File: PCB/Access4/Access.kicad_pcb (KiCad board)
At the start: 2 copper layers, 57.8 x 27 mm, 76 parts, among them J1 USB-C, J2 RFID, J3 INPUTS, J4 Shelly, J5 POWER, J6 DOOR2, J7 DOOR1, Q1 NX7002AK, Q2 PMF250XNEX, SW1 ESE13V01D, U1 ESP32-PICO-MINI-02, U2 FT231XQ, U3 G3VM-41GR8, U4 LMR16006XDDCR, U5 LMR16006XDDCR, U6 AA, U7 QR, U8 G3VM-41GR8, U9 AA

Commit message: Started on Access4
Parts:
- removed C10, C13: 2.2uF, RevK:C_0805_
- removed C11, C14: 10uF, RevK:C_0805_
- removed C12, C9: 100nF, RevK:C_0603_
- removed D6, D7: Schottky, RevK:D_1206_
- removed J4: Shelly, RevK:Shelly
- removed L1, L2: 6.8uH, RevK:L_4x4_
- removed Q1: NX7002AK, Package_TO_SOT_SMD:SOT-23
- removed R20: 100K, RevK:R_0603
- removed R21, R22: 100k 1%, RevK:R_0603
- removed R23: 18k 1%, RevK:R_0603
- removed R24: 30k 1%, RevK:R_0603
- removed R3: 10k, RevK:R_0603
- removed U4, U5: LMR16006XDDCR, RevK:SOT-23-Thin-6-Reg
- added C18: 100nF, RevK:C_0402, F.Cu at (58.9, 101.5)
- added C19: 22uF, RevK:C_0402, F.Cu at (58.9, 103.3)
- added C20: 1uF, RevK:C_0402, F.Cu at (58.9, 105.1)
- added C21: 10uF 50V, RevK:C_0603_, F.Cu at (59.0, 95.8)
- added C22: 10uF 6.3V, RevK:C_0603_, F.Cu at (59.0, 97.7)
- added C23: 100nF, RevK:C_0603_, F.Cu at (59.0, 99.6)
- added J8: Shelly, RevK:Shelly, F.Cu at (47.2, 107.9)
- added L3: 10uH, RevK:L_4x4_, F.Cu at (60.2, 87.1)
- added L4: 10uH, RevK:L_4x4_, F.Cu at (60.2, 92.2)
- added PCB1: 70x70, RevK:PCB7070, F.Cu at (98.0, 102.0)
- added R26: 10K, RevK:R_0402, F.Cu at (61.5, 101.5)
- added R27: 1M, RevK:R_0402_, F.Cu at (61.5, 103.3)
- added U10: ESP32-S3-MINI-1, RevK:ESP32-S3-MINI-1, F.Cu at (91.9, 125.3)
- added V1: ~, RevK:VCUT70, F.Cu at (103.0, 62.4)
- added V2: ~, RevK:VCUT70, F.Cu at (103.0, 64.7)
- C1: value 0.1uF -> 10uF 50V; footprint RevK:C_0603 -> RevK:C_0603_
- C15: value 1uF -> 10uF 6.3V; footprint RevK:C_0603 -> RevK:C_0603_
- C16: value 10nF -> 100nF; footprint RevK:C_0603 -> RevK:C_0603_
- C2, C3, C4, C5, C6, C7, C8, D1, D2, D3, D4: moved to F.Cu
- R1: value 10k -> 124k; footprint RevK:R_0603 -> RevK:R_0402_
- R14: value 27R -> 124k; footprint RevK:R_0603 -> RevK:R_0402_
- R15: value 27R -> 39k2; footprint RevK:R_0603 -> RevK:R_0402_
- R2: value 4k7 -> 23k2; footprint RevK:R_0603 -> RevK:R_0402_
- U1: value ESP32-PICO-MINI-02 -> MD8942; footprint RevK:ESP32-PICO-MINI-02 -> RevK:SOT-23-6-MD8942
- U2: value FT231XQ -> MD8942; footprint RevK:QFN-20-1EP_4x4mm_P0.5mm_EP2.5x2.5mm -> RevK:SOT-23-6-MD8942
- moved D1 69.4 mm to (49.5, 81.2), turned to 180 degrees
- moved C2 67.4 mm to (50.5, 78.7)
- moved C3 63.5 mm to (52.5, 78.7)
- moved D2 61.5 mm to (53.5, 81.2), turned to 180 degrees
- moved C4 59.6 mm to (54.5, 78.7)
- moved C5 55.6 mm to (56.5, 78.7)
- moved D3 53.7 mm to (57.5, 81.2), turned to 180 degrees
- moved C6 51.7 mm to (58.5, 78.7)
- moved C7 47.8 mm to (60.5, 78.7)
- moved D4 45.9 mm to (61.5, 81.2), turned to 180 degrees
- moved U2 45.3 mm to (125.3, 125.5)
- moved C8 43.9 mm to (62.5, 78.7)
- moved U1 40.0 mm to (112.0, 125.7)
- moved C17 38.5 mm to (118.1, 98.4)
- moved AJK1 38.5 mm to (77.6, 106.8)
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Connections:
- J1 pad A6: Net-(J1-D+-PadA6) -> D+
- J1 pad A7: Net-(J1-D--PadA7) -> D-
- J1 pad B6: Net-(J1-D+-PadA6) -> D+
- J1 pad B7: Net-(J1-D--PadA7) -> D-
- U1 pad 1: GND -> unconnected-(U1-Pad1)
- U1 pad 3: +3.3V -> unconnected-(U1-Pad3)
- U1 pad 4: unconnected-(U1-I36-Pad4) -> SHDN
- U1 pad 5: unconnected-(U1-I37-Pad5) -> +12V
- U1 pad 7: unconnected-(U1-I39-Pad7) -> GND
- U1 pad 8: EN -> +5V
- U2 pad 1: O -> unconnected-(U2-Pad1)
- U2 pad 3: GND -> unconnected-(U2-Pad3)
- U2 pad 4: GND -> unconnected-(U2-EN-Pad4)
- U2 pad 5: GND -> +12V
- U2 pad 6: GND -> unconnected-(U2-Pad6)
- U2 pad 7: Net-(U2-CBUS2) -> GND
- U2 pad 8: D+ -> +3.3V
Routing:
- net +3.3V: track 156.1 -> 0.00 mm, vias 10 -> 0
- net +12V: track 69.4 -> 0.00 mm, vias 2 -> 0
- net I: track 58.5 -> 0.00 mm, vias 2 -> 0
- net O: track 57.1 -> 0.00 mm, vias 2 -> 0
- net BOOT: track 54.3 -> 0.00 mm, vias 2 -> 0
- net R: track 43.2 -> 0.00 mm, vias 2 -> 0
- net B: track 42.0 -> 0.00 mm, vias 2 -> 0
- net G: track 40.3 -> 0.00 mm, vias 2 -> 0
- net GND: track 36.2 -> 0.00 mm, vias 13 -> 0
- net EN: track 35.8 -> 0.00 mm, vias 2 -> 0
- net RELAY1: track 34.5 -> 0.00 mm, vias 2 -> 0
- net RELAY2: track 32.1 -> 0.00 mm, vias 2 -> 0
- net TAMPER: track 29.5 -> 0.00 mm, vias 2 -> 0
- net Net-(Q1-D): track 27.5 -> 0.00 mm, vias 2 -> 0
- net +5V: track 25.3 -> 0.00 mm, vias 2 -> 0
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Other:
- board size 57.8 x 27 mm -> 70 x 70 mm

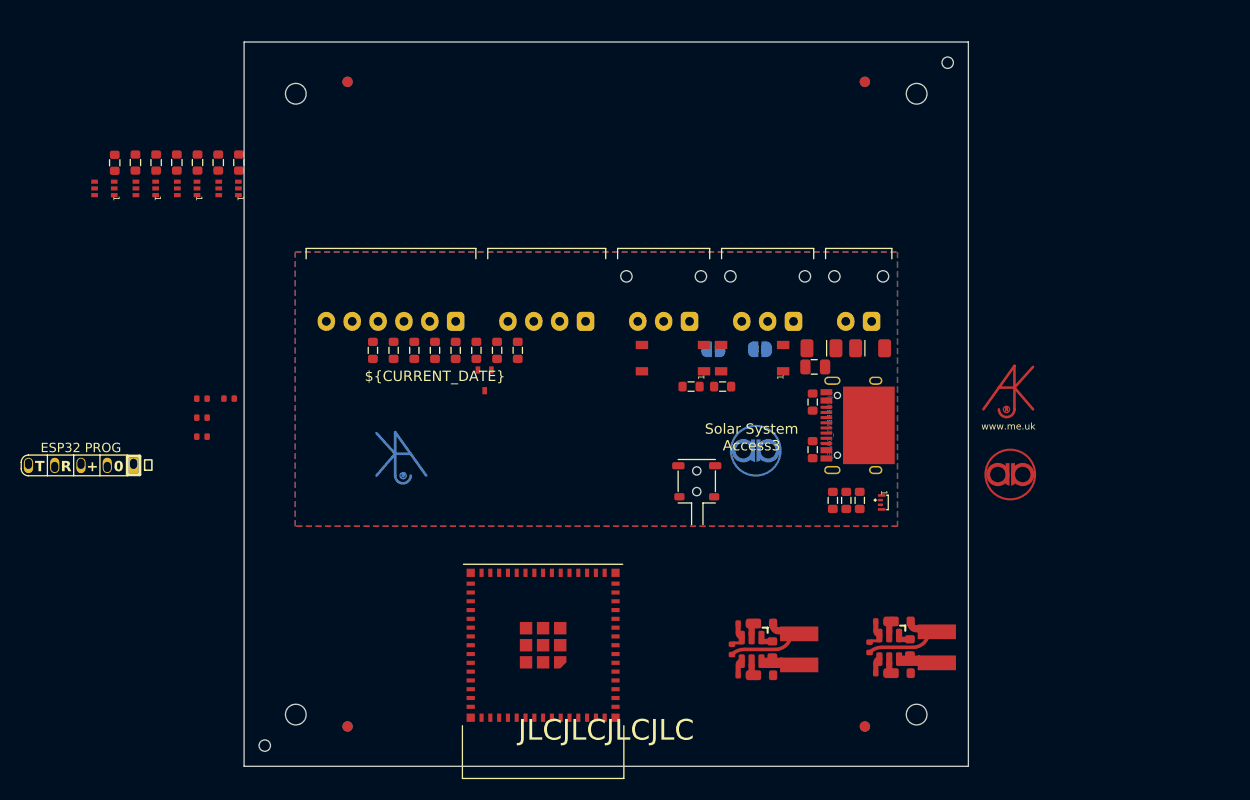
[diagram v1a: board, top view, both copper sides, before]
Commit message: Basic size and placement
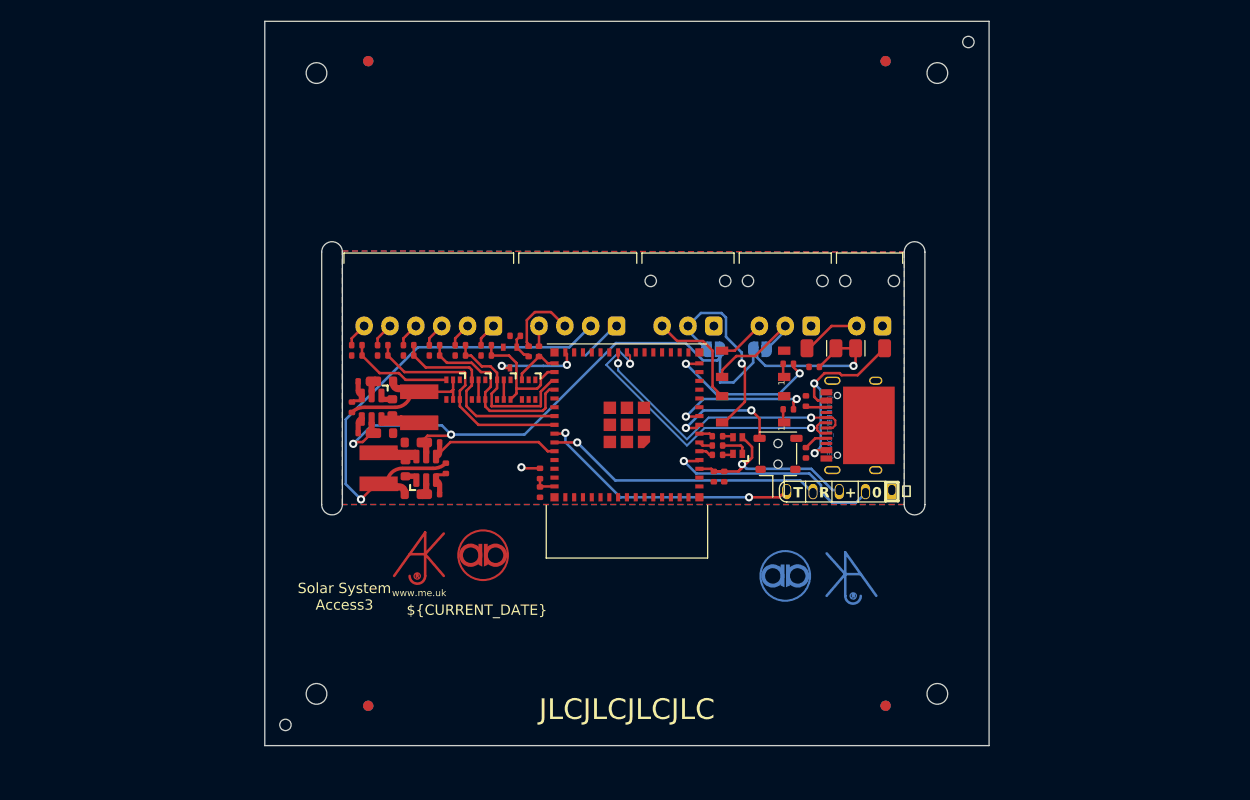
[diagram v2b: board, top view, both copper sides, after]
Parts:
- removed D5: LED_BARG, RevK:MHS190RGBCT
- removed R17: 300R, RevK:R_0603
- removed R18: 1K, RevK:R_0603
- removed R19: 100R, RevK:R_0603
- added D6: RGB, RevK:LED-RGB-1.6x1.6, F.Cu at (110.7, 106.0)
- added R20: 2K, RevK:R_0402, F.Cu at (108.8, 106.9)
- added R21: 220R, RevK:R_0402, F.Cu at (108.8, 105.1)
- added R3: 680R, RevK:R_0402, F.Cu at (108.8, 106.0)
- C17: footprint RevK:C_0805 -> RevK:C_0402
- C2, C3, C4, C5, C6, C7, C8: footprint RevK:C_0603 -> RevK:C_0402
- D1, D2, D3, D4: footprint Package_TO_SOT_SMD:SOT-363_SC-70-6 -> RevK:SOT-363_SC-70-6
- R10, R11, R12, R13, R16, R25, R4, R5, R6, R7, R8, R9: footprint RevK:R_0603 -> RevK:R_0402
- moved J8 73.3 mm to (120.5, 110.5)
- moved Logo1 59.2 mm to (80.5, 116.5)
- moved U2 55.1 mm to (75.3, 102.3)
- moved U9 51.5 mm to (86.1, 116.6)
- moved C19 50.8 mm to (109.4, 109.0), turned to -90 degrees
- moved C18 50.0 mm to (108.4, 109.0), turned to -90 degrees
- moved V2 47.1 mm to (100.0, 111.7), turned to 180 degrees
- moved D1 45.4 mm to (90.5, 100.6), turned to -90 degrees
- moved AJK1 45.0 mm to (121.1, 118.4)
- moved C2 42.2 mm to (89.2, 95.4), turned to 0 degrees
- moved D2 39.7 mm to (88.1, 100.6), turned to -90 degrees
- moved C16 39.6 mm to (52.0, 100.0)
- moved C3 38.7 mm to (86.4, 97.3), turned to 180 degrees
- moved U1 36.0 mm to (80.6, 108.2), turned to -90 degrees
- moved C4 34.8 mm to (83.9, 97.3), turned to 180 degrees
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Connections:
- U10 pad 15: unconnected-(U10-GPIO11-Pad15) -> RELAY1
- U10 pad 30: unconnected-(U10-GPIO48-Pad30) -> RFRX
- U10 pad 31: unconnected-(U10-GPIO35-Pad31) -> RFTX
- U10 pad 32: unconnected-(U10-GPIO36-Pad32) -> IO1
- U10 pad 33: unconnected-(U10-GPIO37-Pad33) -> IO2
- U10 pad 34: unconnected-(U10-GPIO38-Pad34) -> IO3
- U10 pad 35: unconnected-(U10-GPIO39-Pad35) -> IO4
- U10 pad 36: unconnected-(U10-GPIO40-Pad36) -> IO5
- U10 pad 37: unconnected-(U10-GPIO41-Pad37) -> IO6
- U10 pad 41: unconnected-(U10-GPIO45-Pad41) -> SHDN
- U10 pad 5: unconnected-(U10-GPIO1-Pad5) -> G
- U10 pad 6: unconnected-(U10-GPIO2-Pad6) -> R
- U10 pad 7: unconnected-(U10-GPIO3-Pad7) -> B
- U10 pad 8: unconnected-(U10-GPIO4-Pad8) -> TAMPER
- U10 pad 9: unconnected-(U10-GPIO5-Pad9) -> RELAY2
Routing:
- net +12V: track 0.00 -> 72.5 mm, vias 0 -> 3
- net +5V: track 0.00 -> 38.1 mm, vias 0 -> 1
- net D-: track 0.00 -> 31.4 mm, vias 0 -> 2
- net +3.3V: track 0.00 -> 31.3 mm, vias 0 -> 2
- net D+: track 0.00 -> 27.9 mm, vias 0 -> 2
- net Net-(J8-Rx): track 0.00 -> 27.0 mm, vias 0 -> 1
- net Net-(J8-Tx): track 0.00 -> 25.9 mm, vias 0 -> 2
- net IO5: track 0.00 -> 22.5 mm
- net Net-(J8-0): track 0.00 -> 21.5 mm, vias 0 -> 1
- net IO4: track 0.00 -> 19.8 mm
- net VBUS: track 0.00 -> 19.5 mm, vias 0 -> 2
- net Net-(J6-Pin_2): track 0.00 -> 19.3 mm, vias 0 -> 1
- net IO3: track 0.00 -> 18.6 mm
- net IO2: track 0.00 -> 16.1 mm
- net RELAY1: track 0.00 -> 15.6 mm, vias 0 -> 2
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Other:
- board text removed: "-"
- board text removed: "Door Closed"
- board text removed: "Exit Button"
- board text removed: "Lock Engaged"
- board text removed: "Power"

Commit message: Basic layout better
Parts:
- moved D4 8.03 mm to (87.3, 107.5), turned to 0 degrees
- moved D3 4.79 mm to (87.3, 105.1), turned to 0 degrees
- moved D1 3.21 mm to (87.3, 100.3), turned to 0 degrees
- moved D2 2.25 mm to (87.3, 102.7), turned to 0 degrees
- moved U9 1.61 mm to (87.5, 117.4)
- moved C8 0.30 mm to (74.2, 97.3)
- moved R13 0.30 mm to (74.2, 96.3)
- moved R5 0.10 mm to (117.4, 101.7)
- moved R4 0.10 mm to (117.2, 106.7)
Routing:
- net +3.3V: track 31.3 -> 92.5 mm, vias 2 -> 8
- net GND: track 4.44 -> 28.2 mm, vias 0 -> 12
- net IO6: track 10.1 -> 31.8 mm
- net +12V: track 72.5 -> 79.2 mm
- net RFTX: track 4.79 -> 9.53 mm
- net IO4: track 19.8 -> 24.2 mm
- net IO5: track 22.5 -> 26.7 mm
- net IO2: track 16.1 -> 18.5 mm
- net IO1: track 12.2 -> 14.4 mm
- net SHDN: track 12.4 -> 13.9 mm
- net Net-(J8-0): track 21.5 -> 20.4 mm, vias 1 -> 2
- net IO3: track 18.6 -> 19.5 mm
- net Net-(J6-Pin_2): track 19.3 -> 18.6 mm
- net Net-(J8-Rx): track 27.0 -> 27.5 mm

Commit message: Crashing KiCad
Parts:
- moved C15 47.8 mm to (58.9, 104.3)
- moved R14 45.5 mm to (61.2, 108.6)
- moved R15 44.1 mm to (63.0, 111.6)
- moved C1 43.8 mm to (56.2, 107.3)
- moved R1 43.1 mm to (60.9, 105.5)
- moved U7 34.8 mm to (94.2, 123.2)
- moved J8 1.56 mm to (119.0, 110.5)
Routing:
- net +12V: track 79.2 -> 75.5 mm
- net GND: track 28.2 -> 30.9 mm
- net +3.3V: track 92.5 -> 89.9 mm
- net Net-(J8-Tx): track 25.9 -> 23.6 mm, vias 2 -> 1
- net Net-(J8-Rx): track 27.5 -> 25.7 mm
- net Net-(J8-0): track 20.4 -> 18.7 mm
- net D-: track 31.4 -> 30.8 mm

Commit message: Tracked (not pretty yet).
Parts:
- removed AJK1: AJK, RevK:AJK
- removed U6: AA, RevK:AA
- Logo1, U9: moved to B.Cu
- moved R2 45.0 mm to (81.4, 110.7)
- moved U7 35.1 mm to (123.7, 104.0)
- moved C16 27.8 mm to (78.6, 108.2)
- moved L3 26.4 mm to (76.0, 108.2), turned to -90 degrees
- moved Logo1 23.2 mm to (99.5, 103.2), turned to 180 degrees
- moved C1 23.2 mm to (79.3, 105.7), turned to 0 degrees
- moved L4 22.1 mm to (79.9, 102.3), turned to 90 degrees
- moved R1 21.8 mm to (82.5, 108.2), turned to -90 degrees
- moved C15 21.4 mm to (79.3, 110.7), turned to 0 degrees
- moved C21 19.8 mm to (76.6, 104.8), turned to 180 degrees
- moved C23 18.5 mm to (77.3, 102.3), turned to 90 degrees
- moved C22 17.7 mm to (76.6, 99.8), turned to 180 degrees
- moved R15 16.5 mm to (74.5, 99.8)
- moved R14 13.7 mm to (73.4, 102.3), turned to 90 degrees
- moved R27 13.0 mm to (74.5, 104.8), turned to 180 degrees
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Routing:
- net GND: vias 12 -> 11

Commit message: Track tidy
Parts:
- moved U9 30.2 mm to (109.5, 103.5), turned to 90 degrees
- moved Logo1 24.0 mm to (123.5, 103.5), turned to 90 degrees
- moved U7 20.7 mm to (103.0, 103.5)
- moved R16 5.64 mm to (110.0, 103.2), turned to 90 degrees
- moved R25 5.24 mm to (114.4, 103.2), turned to 90 degrees
- moved U3 3.41 mm to (110.0, 99.9), turned to 0 degrees
- moved R26 3.32 mm to (89.2, 111.0), turned to 0 degrees
- moved U8 2.84 mm to (114.4, 99.9), turned to 0 degrees
- moved C20 0.78 mm to (91.0, 111.0), turned to 0 degrees
- moved C17 0.67 mm to (118.7, 98.1)
- moved C23 0.20 mm to (77.1, 102.3)
- moved L4 0.20 mm to (79.7, 102.3)
- moved R14 0.20 mm to (73.2, 102.3)
- moved R15 0.20 mm to (74.3, 99.8)
- moved U2 0.20 mm to (75.1, 102.3)
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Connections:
- U10 pad 11: unconnected-(U10-GPIO7-Pad11) -> RELAY2
- U10 pad 12: unconnected-(U10-GPIO8-Pad12) -> RELAY1
- U10 pad 15: RELAY1 -> unconnected-(U10-GPIO11-Pad15)
- U10 pad 9: RELAY2 -> unconnected-(U10-GPIO5-Pad9)
- U3 pad 3: Net-(J6-Pin_3) -> Net-(J6-Pin_2)
- U3 pad 4: Net-(J6-Pin_2) -> Net-(J6-Pin_3)
- U8 pad 3: Net-(J7-Pin_3) -> Net-(J7-Pin_2)
- U8 pad 4: Net-(J7-Pin_2) -> Net-(J7-Pin_3)
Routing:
- net RELAY2: track 13.8 -> 3.66 mm, vias 2 -> 0
- net +5V: track 37.7 -> 44.8 mm
- net RELAY1: track 15.6 -> 8.51 mm, vias 2 -> 0
- net GND: track 30.9 -> 24.3 mm, vias 11 -> 10
- net Net-(J7-Pin_2): track 11.1 -> 5.31 mm
- net D-: track 30.8 -> 25.7 mm
- net TAMPER: track 11.5 -> 6.38 mm, vias 2 -> 0
- net Net-(J6-Pin_3): track 10.7 -> 6.06 mm
- net +3.3V: track 89.9 -> 85.5 mm
- net Net-(J6-Pin_2): track 18.6 -> 14.8 mm, vias 1 -> 0
- net D+: track 27.6 -> 25.1 mm
- net Net-(J2-Pin_3): track 6.95 -> 9.03 mm
- net Net-(J7-Pin_3): track 4.59 -> 2.54 mm
- net Net-(J8-Tx): track 23.6 -> 21.8 mm
- net Net-(U10-EN): track 2.15 -> 3.65 mm
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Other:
- board text added: "3"
- board text added: "4"
- board text added: "6"
- board text added: "Access4"
- board text added: "General I/O"
- board text added: "Solar System"
- board text added: "Solar System Access4"
- board text removed: "General I/O 1-6"
- board text removed: "Solar System Access3"
